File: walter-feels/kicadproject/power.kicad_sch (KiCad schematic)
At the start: 36 parts, among them U11 LT3120JV#PBF, U12 MAX17291ATA+T

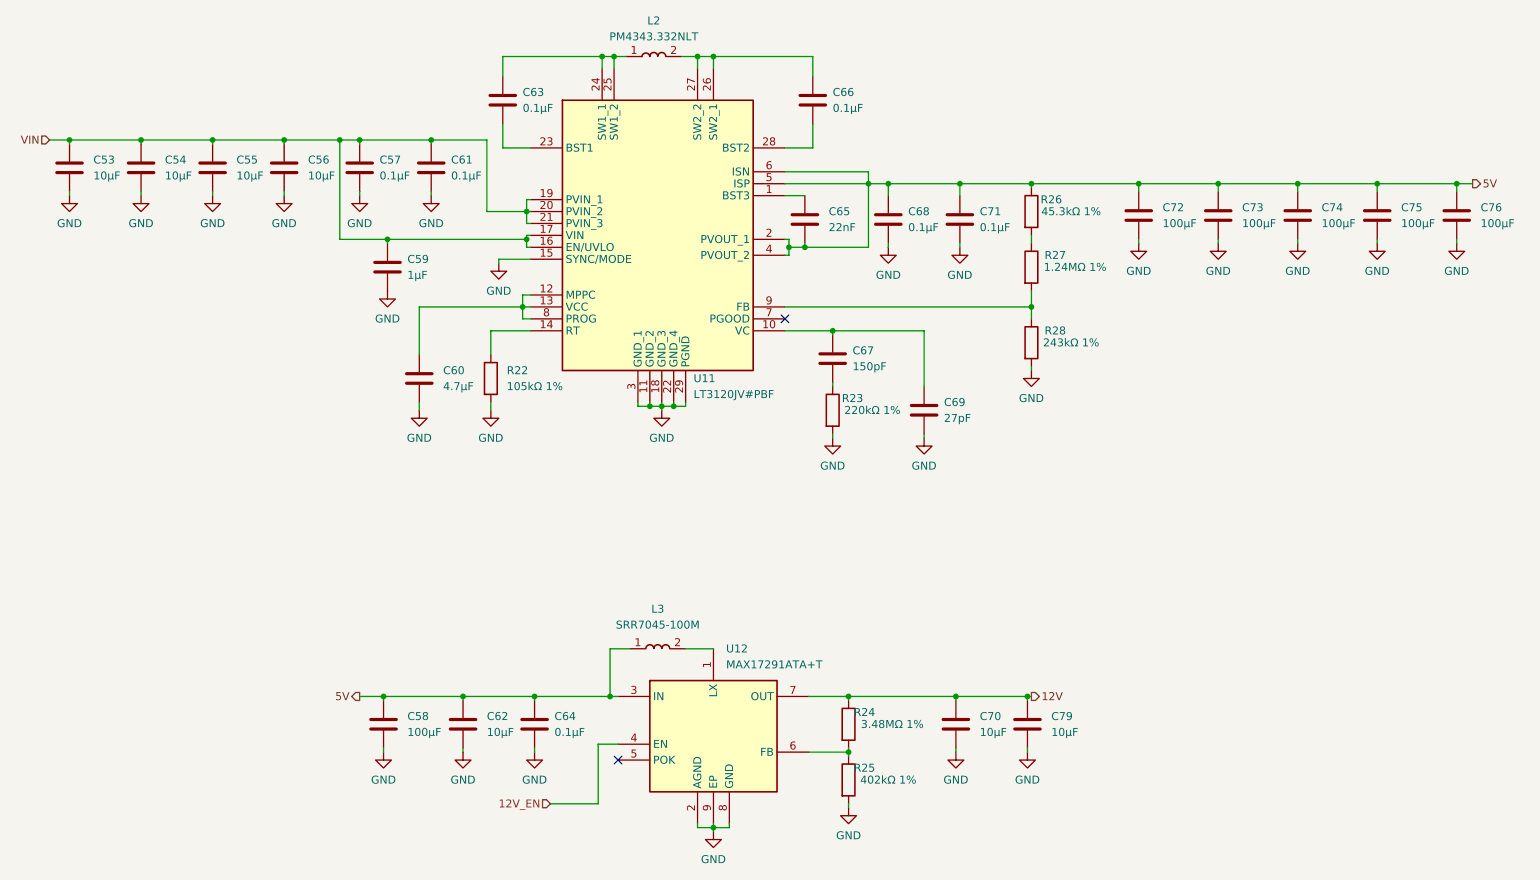
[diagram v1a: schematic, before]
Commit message: Updated Walter Feels to V2.3
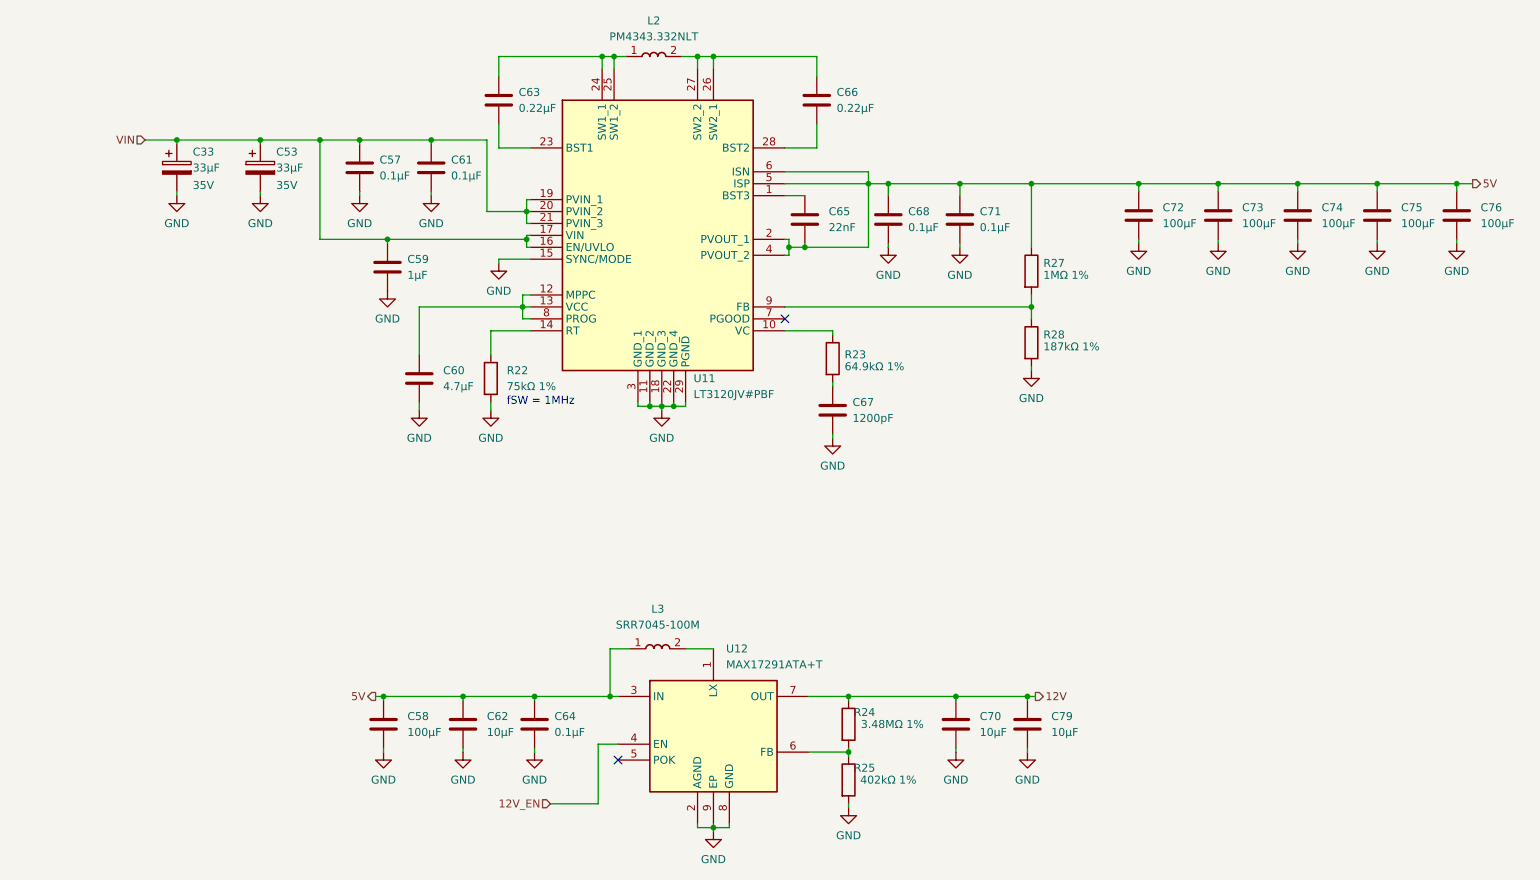
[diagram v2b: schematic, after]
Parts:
- removed C53, C54, C55, C56: 10µF, Capacitor_SMD:C_1206_3216Metric, symbol Device:C
- removed C69: 27pF, Capacitor_SMD:C_0603_1608Metric, symbol Device:C
- removed R26: 45.3kΩ 1%, Resistor_SMD:R_0603_1608Metric, symbol Device:R
- added C33, C53: 33µF, Capacitor_Tantalum_SMD:CP_EIA-7343-30_AVX-N, symbol Device:C_Polarized
- C63, C66: value 0.1µF -> 0.22µF; JLCPCB C14663 -> C21120
- C67: value 150pF -> 1200pF; JLCPCB C1594 -> C30615
- R22: value 105kΩ 1% -> 75kΩ 1%; JLCPCB C325596 -> C23242
- R23: value 220kΩ 1% -> 64.9kΩ 1%; JLCPCB C22961 -> C14891
- R27: value 1.24MΩ 1% -> 1MΩ 1%; JLCPCB C910921 -> C22935
- R28: value 243kΩ 1% -> 187kΩ 1%; JLCPCB C100895 -> C321764
- U11: JLCPCB (none) -> C3198178
- U12: JLCPCB (none) -> C7456683
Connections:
- net 5V: now also R27.1
- net GND: now also C67.2, C33.2, C53.2; no longer R23.2
- net VIN: now also C33.1, C53.1
- net at U11.10 (VC): now also R23.1; no longer C67.1
- new net: C67.1, R23.2
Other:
- note added: "fSW = 1MHz"
- moved on the sheet: C63, C66, C67, R23

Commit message: Updated Walter Feels project to version 2.6
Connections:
- net SYSPOWER_GOOD: now reaches U11.7 (PGOOD)
- no-connect marks 2 -> 1
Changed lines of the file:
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@@
   (title_block
     (title "Walter Feels")
-    (date "2025-02-12")
-    (rev "2.4")
+    (date "2026-01-13")
+    (rev "2.6")
     (company "DPTechnics BV")
     (comment 1 "Checked by: Jonas Maes")
@@
   )
   (no_connect (at 123.825 140.97))
-  (no_connect (at 150.495 70.485))
+  (wire (pts (xy 257.81 47.625) (xy 257.81 48.895))
+    (stroke (width 0) (type default) (color 0 0 0 0))
+  )
   (wire (pts (xy 127 83.82) (xy 127 84.455))
     (stroke (width 0) (type default) (color 0 0 0 0))
@@
   )
   (wire (pts (xy 86.36 131.445) (xy 86.36 130.81))
+    (stroke (width 0) (type default) (color 0 0 0 0))
+  )
+  (wire (pts (xy 150.495 70.485) (xy 152.4 70.485))
     (stroke (width 0) (type default) (color 0 0 0 0))
   )
@@
   (text "fSW = 1MHz" (at 106.045 84.455 0)
     (effects (font (size 1.27 1.27)) (justify left bottom))
+  )
+  (hierarchical_label "SYSPOWER_GOOD" (shape output) (at 152.4 70.485 0)
+    (effects (font (size 1.27 1.27)) (justify left))
   )
   (hierarchical_label "VIN" (shape input) (at 48.26 41.91 180)
@@
     (pin "2")
   )
+  (symbol (lib_id "power:PWR_FLAG") (at 257.81 47.625 0) (unit 1)
+    (in_bom yes) (on_board yes)
+    (property "Reference" "#FLG0101" (id 0) (at 257.81 45.72 0)
+      (effects (font (size 1.27 1.27)) hide)
+    )
+    (property "Value" "PWR_FLAG" (id 1) (at 257.81 43.815 0))
+    (property "Footprint" "" (id 2) (at 257.81 47.625 0)
+      (effects (font (size 1.27 1.27)) hide)
+    )
+    (property "Datasheet" "~" (id 3) (at 257.81 47.625 0)
+      (effects (font (size 1.27 1.27)) hide)
+    )
+    (pin "1")
+  )
   (symbol (lib_id "LT3120JV#PBF:LT3120JV#PBF") (at 130.81 55.88 0) (unit 1)
